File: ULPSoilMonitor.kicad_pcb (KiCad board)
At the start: 2 copper layers, 27.1 x 76.2 mm, 51 parts, among them J1 Conn_01x03_Male, J2 Conn_01x03_Male, J3 Conn_01x03_Male, J4 Conn_01x03_Male, J5 Conn_01x03_Male, J6 Conn_01x03_Male, J7 USB_B_Micro, J8 BME280_(GYBMEP), Q1 BC807, Q2 MMDT3904, SW1 RESET, U1 ESP32-WROOM-32, U2 UA7BM33, U3 FT231XS, U4 BME280

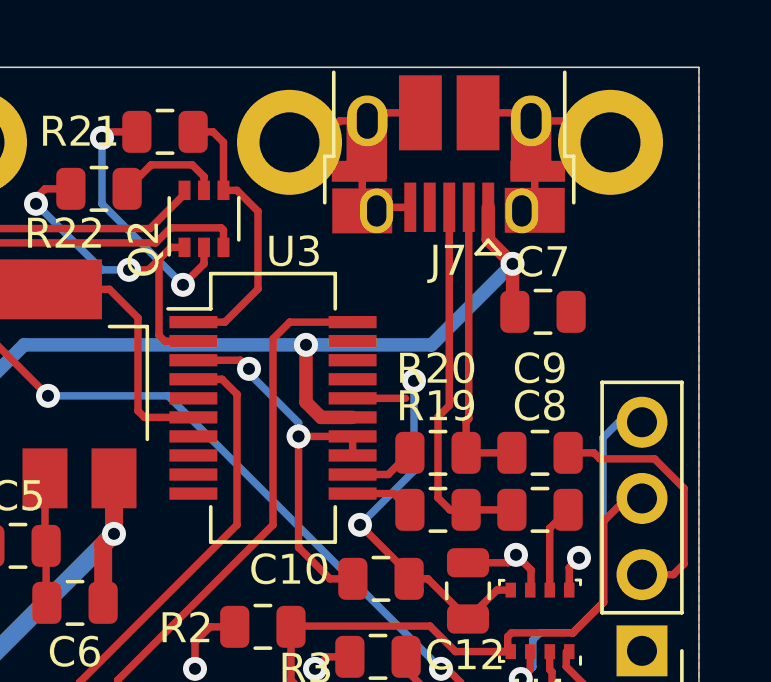
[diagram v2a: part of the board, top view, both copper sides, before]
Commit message: move USB connector further over the edge
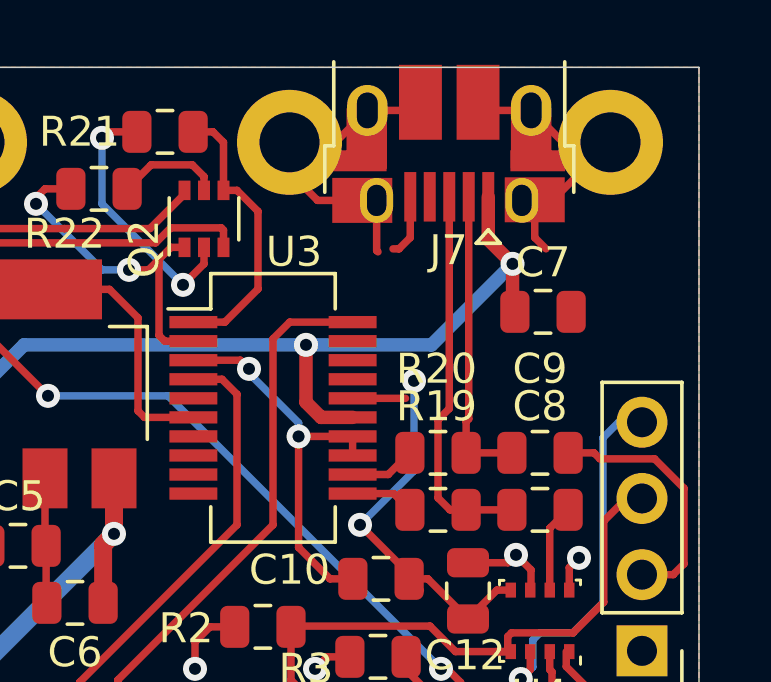
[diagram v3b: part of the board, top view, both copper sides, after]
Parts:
- moved J7 0.35 mm to (57.2, 30.8)
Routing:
- net -BATT: track 60.6 -> 67.8 mm
- net Net-(C8-Pad1): track 12.5 -> 13.2 mm
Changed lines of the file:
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@@
     (thickness 1.6)
     (drawings 7)
-    (tracks 384)
+    (tracks 393)
     (zones 0)
     (modules 51)
@@
   )
   (module Connector_USB:USB_Micro-B_Amphenol_10103594-0001LF_Horizontal (layer F.Cu)
-    (at 57.25 31.15 180)
+    (at 57.25 30.8 180)
     (descr "Micro USB Type B 10103594-0001LF, http://cdn.amphenol-icc.com/media/wysiwyg/files/drawing/10103594.pdf")
     (tags "USB USB_B USB_micro USB_OTG")
@@
   (segment (start 41.45 77.35) (end 41.6 77.2) (width 0.6) (layer B.Cu) (net 1) (status 30))
   (segment (start 41.45 102.15) (end 41.45 77.35) (width 0.6) (layer B.Cu) (net 1) (status 30))
-  (segment (start 54.815 29.765) (end 54.545 30.035) (width 0.25) (layer F.Cu) (net 2) (status 30))
-  (segment (start 56.315 29.765) (end 54.815 29.765) (width 0.25) (layer F.Cu) (net 2) (status 30))
-  (segment (start 59.735 29.765) (end 60.005 30.035) (width 0.25) (layer F.Cu) (net 2) (status 30))
-  (segment (start 58.235 29.765) (end 59.735 29.765) (width 0.25) (layer F.Cu) (net 2) (status 30))
-  (segment (start 54.975 32.915) (end 54.855 33.035) (width 0.25) (layer F.Cu) (net 2) (status 30))
-  (segment (start 55.975 32.915) (end 54.975 32.915) (width 0.25) (layer F.Cu) (net 2) (status 30))
-  (segment (start 61.935 30.035) (end 62.65 30.75) (width 0.25) (layer F.Cu) (net 2) (status 30))
-  (segment (start 60.005 30.035) (end 61.935 30.035) (width 0.25) (layer F.Cu) (net 2) (status 30))
-  (segment (start 52.905 30.75) (end 51.95 30.75) (width 0.25) (layer F.Cu) (net 2) (status 30))
-  (segment (start 53.62 30.035) (end 52.905 30.75) (width 0.25) (layer F.Cu) (net 2) (status 20))
-  (segment (start 54.545 30.035) (end 53.62 30.035) (width 0.25) (layer F.Cu) (net 2) (status 10))
   (segment (start 54.0543 39.2825) (end 55.8175 39.2825) (width 0.25) (layer F.Cu) (net 2) (status 10))
   (segment (start 48.7457 39.9175) (end 47.1175 39.9175) (width 0.25) (layer F.Cu) (net 2) (status 10))
@@
   (segment (start 56.5625 45.3) (end 57.9 46.6375) (width 0.25) (layer F.Cu) (net 2) (status 20))
   (segment (start 55.9375 45.3) (end 56.5625 45.3) (width 0.25) (layer F.Cu) (net 2) (status 10))
-  (segment (start 54.375 30.205) (end 54.545 30.035) (width 0.25) (layer F.Cu) (net 2) (status 30))
-  (segment (start 54.375 33.035) (end 54.375 30.205) (width 0.25) (layer F.Cu) (net 2) (status 30))
-  (segment (start 60.125 30.155) (end 60.005 30.035) (width 0.25) (layer F.Cu) (net 2) (status 30))
-  (segment (start 60.125 33.015) (end 60.125 30.155) (width 0.25) (layer F.Cu) (net 2) (status 30))
   (segment (start 63.7 45.16) (end 63.7 44.9) (width 0.25) (layer B.Cu) (net 2) (status 30))
   (segment (start 64.74 45.16) (end 63.7 45.16) (width 0.25) (layer F.Cu) (net 2) (status 20))
@@
   (segment (start 58.8625 45.675) (end 57.9 46.6375) (width 0.25) (layer F.Cu) (net 2) (status 20))
   (segment (start 59.325 45.675) (end 58.8625 45.675) (width 0.25) (layer F.Cu) (net 2) (status 10))
+  (segment (start 54.855 32.685) (end 54.375 32.685) (width 0.25) (layer F.Cu) (net 2))
+  (segment (start 53.48 30.75) (end 54.545 29.685) (width 0.25) (layer F.Cu) (net 2))
+  (segment (start 51.95 30.75) (end 53.48 30.75) (width 0.25) (layer F.Cu) (net 2))
+  (segment (start 59.715 32.665) (end 59.695 32.685) (width 0.25) (layer F.Cu) (net 2))
+  (segment (start 60.125 32.665) (end 59.715 32.665) (width 0.25) (layer F.Cu) (net 2))
+  (segment (start 60.735 32.665) (end 62.65 30.75) (width 0.25) (layer F.Cu) (net 2))
+  (segment (start 60.125 32.665) (end 60.735 32.665) (width 0.25) (layer F.Cu) (net 2))
+  (segment (start 61.07 30.75) (end 60.005 29.685) (width 0.25) (layer F.Cu) (net 2))
+  (segment (start 62.65 30.75) (end 61.07 30.75) (width 0.25) (layer F.Cu) (net 2))
+  (segment (start 51.95 31.75) (end 51.95 30.75) (width 0.25) (layer F.Cu) (net 2))
+  (segment (start 52.885 32.685) (end 51.95 31.75) (width 0.25) (layer F.Cu) (net 2))
+  (segment (start 54.855 32.685) (end 52.885 32.685) (width 0.25) (layer F.Cu) (net 2))
+  (segment (start 55.975 32.565) (end 55.975 33.925) (width 0.25) (layer F.Cu) (net 2))
+  (segment (start 55.975 33.925) (end 55.6 34.3) (width 0.25) (layer F.Cu) (net 2))
+  (segment (start 55.6 34.3) (end 55.4 34.3) (width 0.25) (layer F.Cu) (net 2))
+  (segment (start 54.855 34.355) (end 54.9 34.4) (width 0.25) (layer F.Cu) (net 2))
+  (segment (start 54.855 32.685) (end 54.855 34.355) (width 0.25) (layer F.Cu) (net 2))
+  (segment (start 60.125 32.665) (end 60.125 33.925) (width 0.25) (layer F.Cu) (net 2))
+  (segment (start 60.125 33.925) (end 60.5 34.3) (width 0.25) (layer F.Cu) (net 2))
+  (segment (start 56.045 29.685) (end 56.315 29.415) (width 0.25) (layer F.Cu) (net 2))
+  (segment (start 54.545 29.685) (end 56.045 29.685) (width 0.25) (layer F.Cu) (net 2))
+  (segment (start 58.505 29.685) (end 58.235 29.415) (width 0.25) (layer F.Cu) (net 2))
+  (segment (start 60.005 29.685) (end 58.505 29.685) (width 0.25) (layer F.Cu) (net 2))
   (segment (start 43.685 68.8225) (end 44.1625 69.3) (width 0.25) (layer F.Cu) (net 3) (status 20))
   (segment (start 43.685 67) (end 43.685 68.8225) (width 0.25) (layer F.Cu) (net 3) (status 10))
@@
   (segment (start 49.58 78.4) (end 46.8375 78.4) (width 0.25) (layer F.Cu) (net 10))
   (segment (start 49.6 78.38) (end 49.58 78.4) (width 0.25) (layer F.Cu) (net 10))
-  (segment (start 58.575 33.99) (end 59.385 34.8) (width 0.45) (layer F.Cu) (net 11))
-  (segment (start 58.575 32.915) (end 58.575 33.99) (width 0.45) (layer F.Cu) (net 11) (status 10))
   (via (at 59.384995 34.799995) (size 0.8) (drill 0.4) (layers F.Cu B.Cu) (net 11))
   (via (at 41.5 40.1) (size 0.8) (drill 0.4) (layers F.Cu B.Cu) (net 11))
@@
   (segment (start 59.384995 36.322495) (end 59.4625 36.4) (width 0.45) (layer F.Cu) (net 11) (status 30))
   (segment (start 59.384995 34.799995) (end 59.384995 36.322495) (width 0.45) (layer F.Cu) (net 11) (status 20))
+  (segment (start 58.575 33.99) (end 59.385 34.8) (width 0.45) (layer F.Cu) (net 11))
+  (segment (start 58.575 32.565) (end 58.575 33.99) (width 0.45) (layer F.Cu) (net 11))
   (segment (start 56.25 70.3) (end 57.35 71.4) (width 0.25) (layer F.Cu) (net 12))
   (segment (start 55.6375 70.3) (end 56.25 70.3) (width 0.25) (layer F.Cu) (net 12))
@@
   (segment (start 46.1 43.8) (end 41.5 48.4) (width 0.6) (layer B.Cu) (net 30))
   (segment (start 41.5 48.4) (end 41.5 72.02) (width 0.6) (layer B.Cu) (net 30) (status 20))
+  (segment (start 59.3625 43) (end 57.8375 43) (width 0.25) (layer F.Cu) (net 31) (status 30))
+  (segment (start 57.275 32.915) (end 57.275 32.565) (width 0.25) (layer F.Cu) (net 31))
+  (segment (start 57.3 43) (end 57.8375 43) (width 0.25) (layer F.Cu) (net 31))
   (segment (start 56.9 42.6) (end 57.3 43) (width 0.25) (layer F.Cu) (net 31))
-  (segment (start 56.9 39.9) (end 56.9 42.6) (width 0.25) (layer F.Cu) (net 31))
-  (segment (start 57.3 43) (end 57.8375 43) (width 0.25) (layer F.Cu) (net 31) (status 20))
-  (segment (start 57.275 32.915) (end 57.275 39.525) (width 0.25) (layer F.Cu) (net 31) (status 10))
-  (segment (start 57.275 39.525) (end 56.9 39.9) (width 0.25) (layer F.Cu) (net 31))
-  (segment (start 59.3625 43) (end 57.8375 43) (width 0.25) (layer F.Cu) (net 31) (status 30))
-  (segment (start 57.925 32.915) (end 57.925 39.96875) (width 0.25) (layer F.Cu) (net 32) (status 10))
-  (segment (start 57.8375 40.05625) (end 57.8375 41.1) (width 0.25) (layer F.Cu) (net 32) (status 20))
+  (segment (start 56.9 40) (end 56.9 42.6) (width 0.25) (layer F.Cu) (net 31))
+  (segment (start 57.275 39.625) (end 56.9 40) (width 0.25) (layer F.Cu) (net 31))
+  (segment (start 57.275 32.565) (end 57.275 39.625) (width 0.25) (layer F.Cu) (net 31))
+  (segment (start 57.8375 41.1) (end 59.3625 41.1) (width 0.25) (layer F.Cu) (net 32) (status 30))
+  (segment (start 57.8375 40.05625) (end 57.8375 41.1) (width 0.25) (layer F.Cu) (net 32))
   (segment (start 57.925 39.96875) (end 57.8375 40.05625) (width 0.25) (layer F.Cu) (net 32))
-  (segment (start 57.8375 41.1) (end 59.3625 41.1) (width 0.25) (layer F.Cu) (net 32) (status 30))
+  (segment (start 57.925 32.565) (end 57.925 39.96875) (width 0.25) (layer F.Cu) (net 32))
   (via (at 50.6 38.3) (size 0.8) (drill 0.4) (layers F.Cu B.Cu) (net 33))
   (segment (start 50.3125 38.0125) (end 50.6 38.3) (width 0.25) (layer F.Cu) (net 33))

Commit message: update drawing to 882a528a10f6fb48f6454efd446c1280f51ad1f8
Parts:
- removed C10: 100nF, Capacitor_SMD:C_0805_2012Metric
- removed JP1: Jumper_3_Bridged12, Connector_PinHeader_2.54mm:PinHeader_1x03_P2.54mm_Vertical
- added D1: CHARGING, LED_SMD:LED_0805_2012Metric, F.Cu at (45.2, 47.5)
- added D2: TX, LED_SMD:LED_0805_2012Metric, F.Cu at (42.9, 39.2)
- added D3: RX, LED_SMD:LED_0805_2012Metric, F.Cu at (42.9, 37.3)
- added Q3: BC817, Package_TO_SOT_SMD:SOT-23, F.Cu at (48.0, 44.7)
- added Q4: MMDT3904, Package_TO_SOT_SMD:SOT-363_SC-70-6, F.Cu at (53.5, 42.0)
- added R23: 1k, Resistor_SMD:R_0805_2012Metric, F.Cu at (41.8, 47.5)
- added R24: 3k9, Resistor_SMD:R_0805_2012Metric, F.Cu at (50.8, 44.2)
- added R25: 2k37, Resistor_SMD:R_0805_2012Metric, F.Cu at (53.6, 44.9)
- added R26: 1k, Resistor_SMD:R_0805_2012Metric, F.Cu at (54.7, 37.8)
- added R27: 22k1, Resistor_SMD:R_0805_2012Metric, F.Cu at (51.8, 34.0)
- added R28: 47k5, Resistor_SMD:R_0805_2012Metric, F.Cu at (54.7, 35.8)
- added R29: R, Resistor_SMD:R_0805_2012Metric, F.Cu at (42.9, 41.1)
- added R30: R, Resistor_SMD:R_0805_2012Metric, F.Cu at (42.9, 35.4)
- C5: value 330nF -> 4.7μF
- C6: value 100nF -> 4.7μF
- C7: value 10nF -> 100nF
- U2: value UA7BM33 -> MCP73123; footprint Package_TO_SOT_SMD:SOT-223-3_TabPin2 -> Package_DFN_QFN:DFN-10-1EP_3x3mm_P0.5mm_EP1.65x2.38mm
- U3: value FT231XS -> CP2102N-A01-GQFN28; footprint Package_SO:QSOP-20_3.9x8.7mm_P0.635mm -> Package_DFN_QFN:QFN-28-1EP_5x5mm_P0.5mm_EP3.35x3.35mm
- moved C6 19.0 mm to (61.3, 36.7), turned to 0 degrees
- moved U2 5.71 mm to (43.5, 44.5), turned to 0 degrees
- moved U3 3.29 mm to (48.3, 38.5), turned to 180 degrees
- moved C5 2.89 mm to (40.1, 43.5), turned to 90 degrees
- moved C7 1.84 mm to (61.3, 34.8)
- moved R1 1.80 mm to (43.3, 71.6), turned to 0 degrees
- moved C2 1.41 mm to (41.2, 89.6), turned to 0 degrees
- moved R20 1.20 mm to (56.9, 39.9)
- moved Q2 0.63 mm to (48.9, 32.7)
- moved R21 0.54 mm to (47.6, 29.9)
- moved R2 0.44 mm to (51.5, 46.9)
- moved R22 0.36 mm to (45.4, 32.0)
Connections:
- C1 pad 1: VCC -> +BATT
- C11 pad 1: VCC -> +BATT
- C12 pad 1: VCC -> +BATT
- C2 pad 1: VCC -> +BATT
- C3 pad 1: VCC -> +BATT
- C5 pad 1: VBUS -> +BATT
- C6 pad 1: +3V3 -> VBUS
- J8 pad 1: VCC -> +BATT
- Q1 pad 2: VCC -> +BATT
- R1 pad 1: VCC -> +BATT
- R2 pad 2: VCC -> +BATT
- R3 pad 2: VCC -> +BATT
- U1 pad 2: VCC -> +BATT
- U2 pad 2: -BATT -> VBUS
- U2 pad 3: +3V3 -> +BATT
- U3 pad 1: DTR -> (no net)
- U3 pad 11: D+ -> (no net)
- U3 pad 12: D- -> (no net)
- U3 pad 13: Net-(C10-Pad1) -> CHREN
- U3 pad 14: Net-(C10-Pad1) -> CHR1
- U3 pad 15: VBUS -> CHR0
- U3 pad 16: -BATT -> (no net)
- U3 pad 18: (no net) -> /USBtoSerial/~RXT
- U3 pad 19: (no net) -> /USBtoSerial/~TXT
- U3 pad 2: RTS -> (no net)
- U3 pad 20: ESPRX -> (no net)
- U3 pad 3: Net-(C10-Pad1) -> -BATT
- U3 pad 4: ESPTX -> D+
- U3 pad 5: (no net) -> D-
- U3 pad 6: -BATT -> /USBtoSerial/VDD
- U3 pad 7: (no net) -> VBUS
- U3 pad 8: (no net) -> Net-(R27-Pad2)
- U3 pad 9: (no net) -> /USBtoSerial/~RSTb
- U4 pad 2: VCC -> +BATT
- U4 pad 6: VCC -> +BATT
- U4 pad 8: VCC -> +BATT
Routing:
- net VCC: track 40.7 -> 0.00 mm, vias 7 -> 0
- net -BATT: track 67.8 -> 103.6 mm, vias 2 -> 1
- net +3V3: track 34.6 -> 0.00 mm, vias 1 -> 0
- net /USBtoSerial/VDD: track 0.00 -> 31.6 mm, vias 0 -> 4
- net VBUS: track 32.8 -> 49.5 mm, vias 3 -> 4
- net CHREN: track 0.00 -> 13.6 mm, vias 0 -> 2
- net CHR1: track 0.00 -> 13.5 mm, vias 0 -> 2
- net Net-(C10-Pad1): track 13.3 -> 0.00 mm, vias 2 -> 0
- net CHR0: track 0.00 -> 13.3 mm, vias 0 -> 2
- net IO0: track 34.5 -> 21.9 mm
- net Net-(R27-Pad2): track 0.00 -> 8.18 mm, vias 0 -> 2
- net DTR: track 9.40 -> 17.2 mm, vias 0 -> 2
- net /USBtoSerial/~RSTb: track 0.00 -> 7.36 mm, vias 0 -> 2
- net Net-(Q3-Pad2): track 0.00 -> 6.36 mm
- net +BATT: track 46.2 -> 40.5 mm, vias 0 -> 10
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- added copper zone on B.Cu, net +BATT
- removed copper zone on B.Cu, net VCC
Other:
- board text added: "Flobs ULPSoilMonitor v2.1 2020-06-26"
- board text removed: "Flobs ULPSoilMonitor v2.0 2020-05-16"

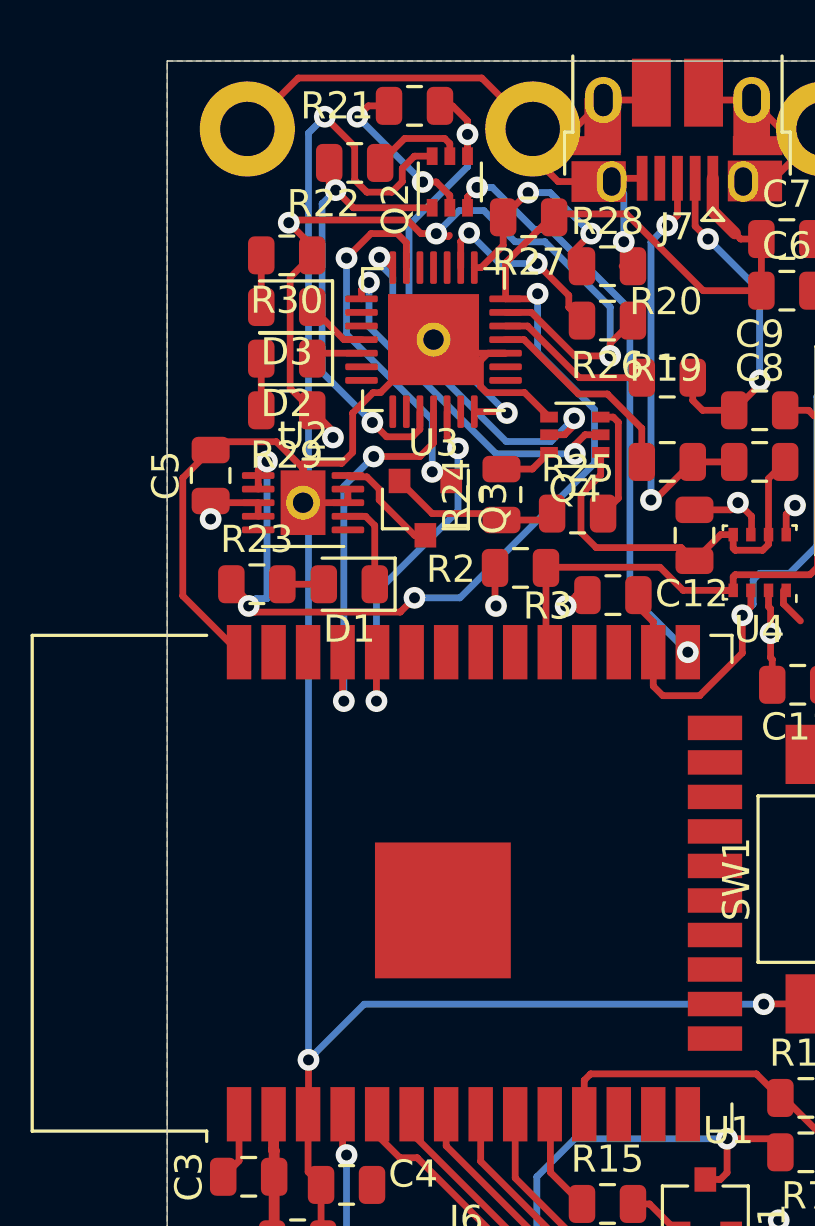
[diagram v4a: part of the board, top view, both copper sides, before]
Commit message: route around vias for soldering
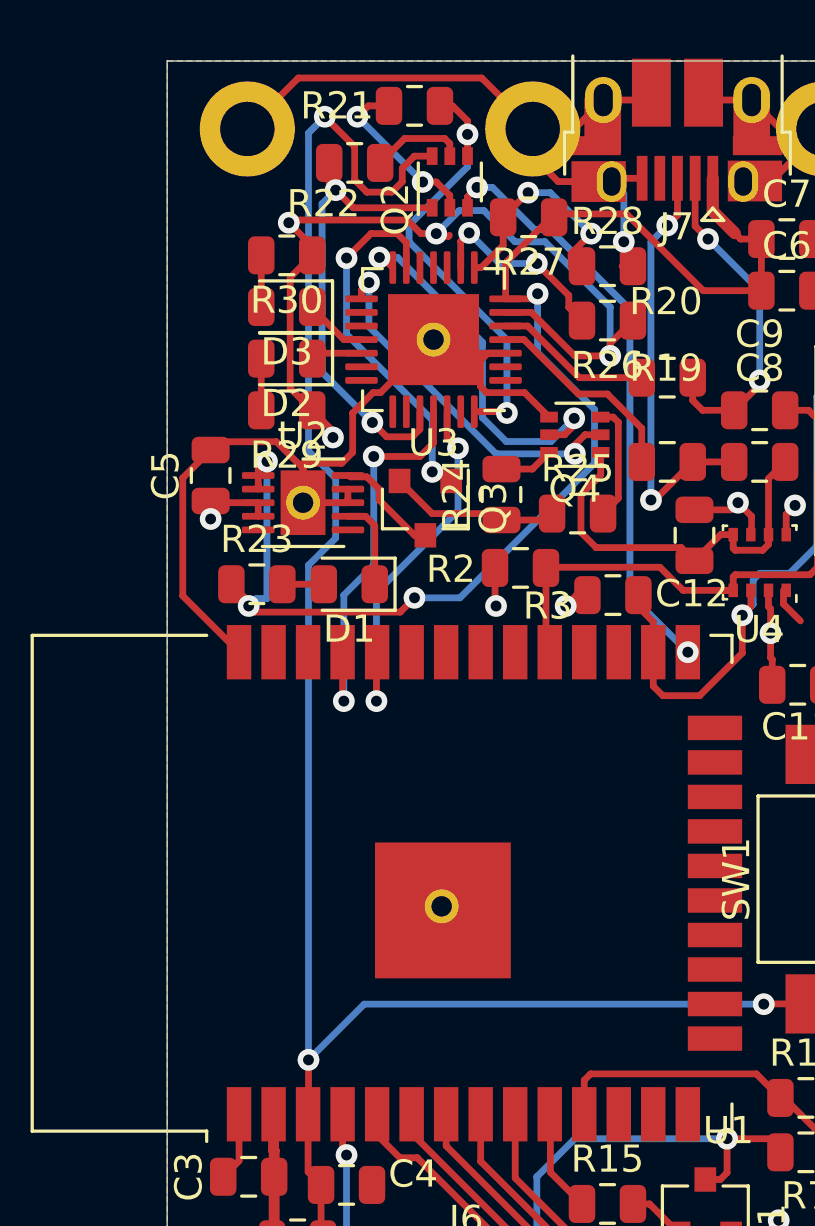
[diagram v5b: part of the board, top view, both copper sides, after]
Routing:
- net EN: track 67.6 -> 68.5 mm
